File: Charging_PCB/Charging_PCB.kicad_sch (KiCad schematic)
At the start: 15 parts, among them K3 BMS_Relay, K4 IMD_Relay, Q1 PMOS, Q2 PMOS, U112 Charger Input, U113 Signal Inputs, U114 Relay Output

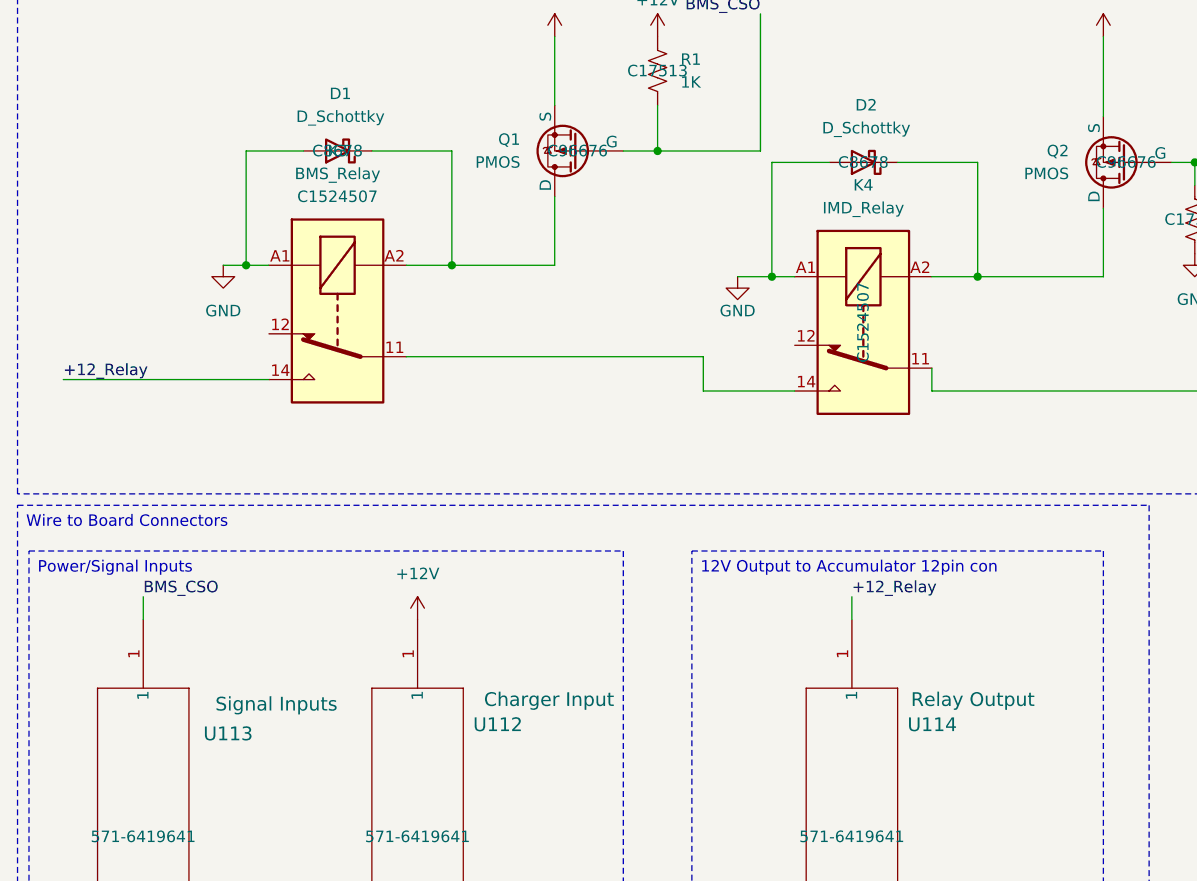
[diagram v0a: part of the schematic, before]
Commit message: Compacted PCB, and finished BOM,CPL,Gerbers(Charging)
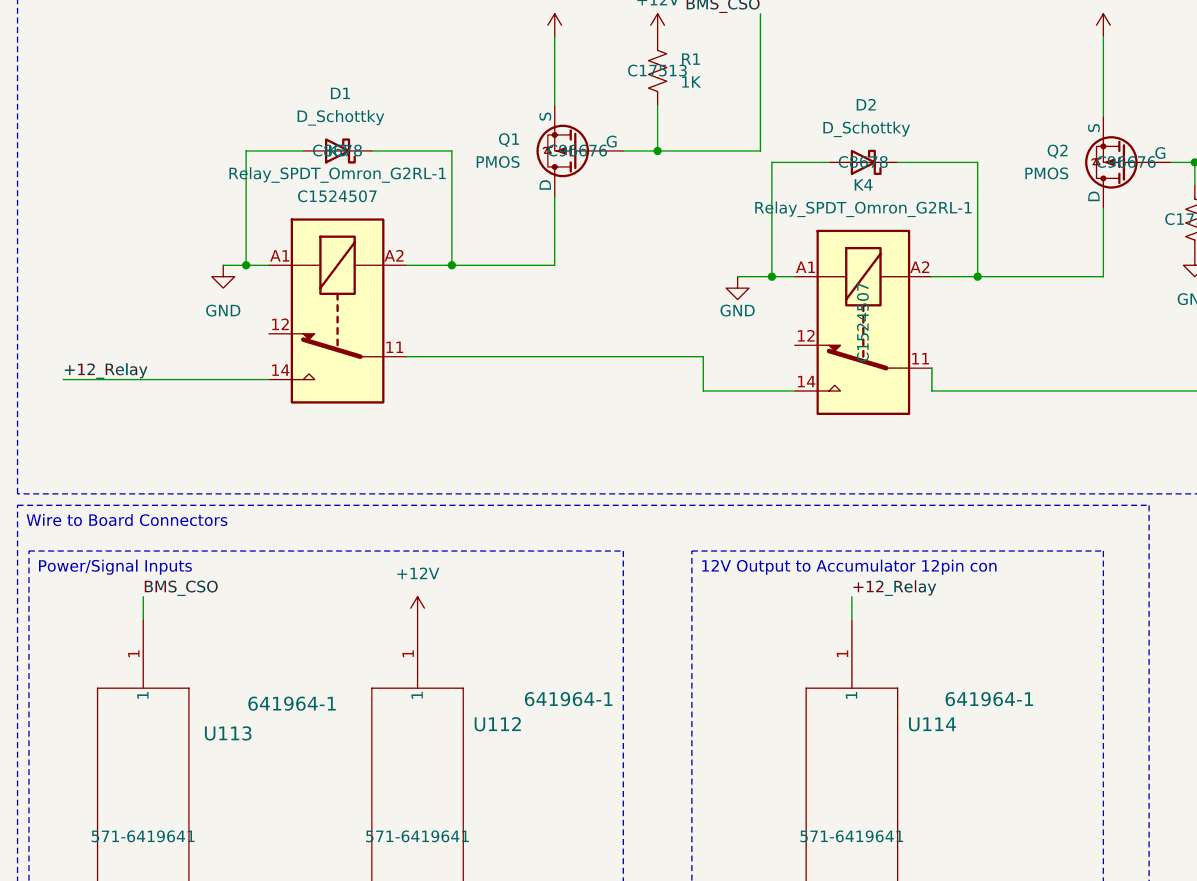
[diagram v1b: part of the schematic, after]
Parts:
- K3: value BMS_Relay -> Relay_SPDT_Omron_G2RL-1
- K4: value IMD_Relay -> Relay_SPDT_Omron_G2RL-1
- U112: value Charger Input -> 641964-1
- U113: value Signal Inputs -> 641964-1
- U114: value Relay Output -> 641964-1
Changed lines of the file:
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@@
 			)
 		)
-		(property "Value" "BMS_Relay"
+		(property "Value" "Relay_SPDT_Omron_G2RL-1"
 			(at 58.42 46.99 90)
 			(effects
@@
 			)
 		)
-		(property "Value" "Relay Output"
+		(property "Value" "641964-1"
 			(at 135.89 105.41 90)
 			(effects
@@
 			)
 		)
-		(property "Value" "IMD_Relay"
+		(property "Value" "Relay_SPDT_Omron_G2RL-1"
 			(at 116.84 50.8 90)
 			(effects
@@
 			)
 		)
-		(property "Value" "Signal Inputs"
+		(property "Value" "641964-1"
 			(at 58.42 105.918 90)
 			(effects
@@
 			)
 		)
-		(property "Value" "Charger Input"
+		(property "Value" "641964-1"
 			(at 89.154 105.41 90)
 			(effects

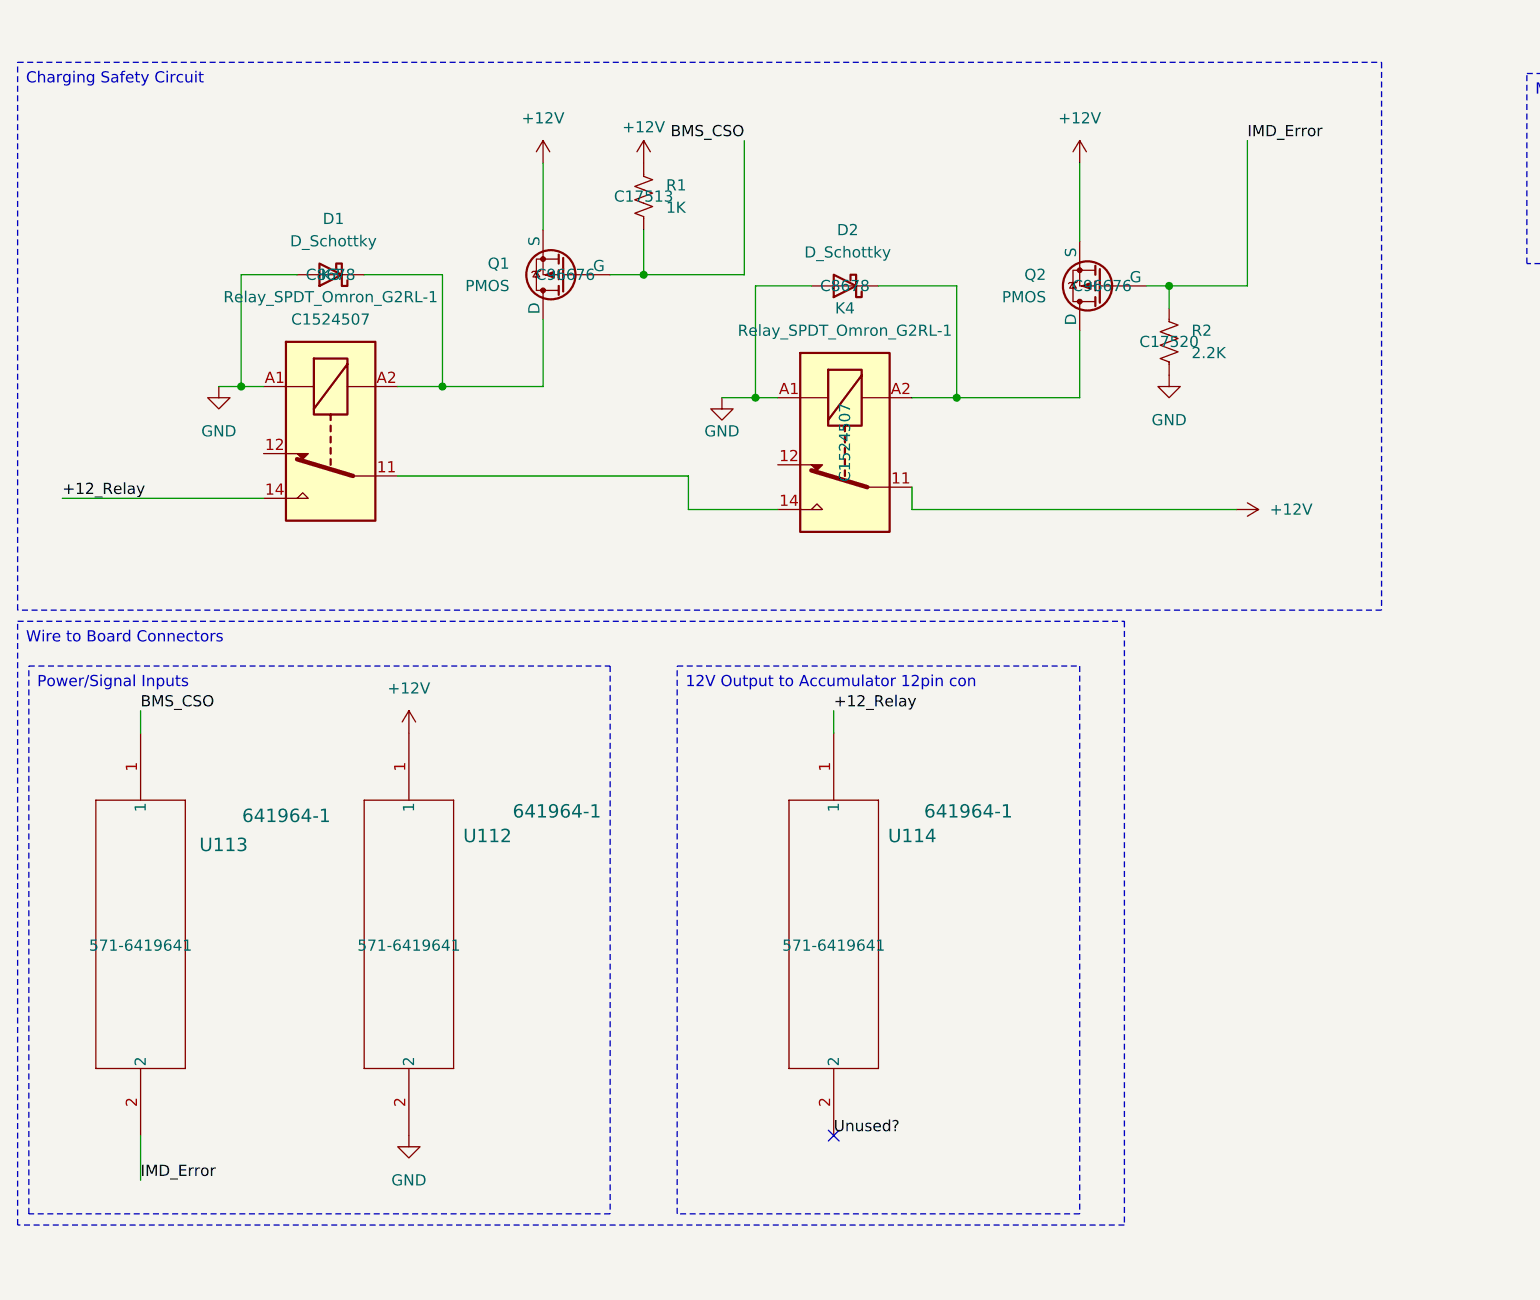
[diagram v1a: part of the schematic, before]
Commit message: Fixed bad PMOS footprint and symbol, fixed gerbers/BOM/CPL
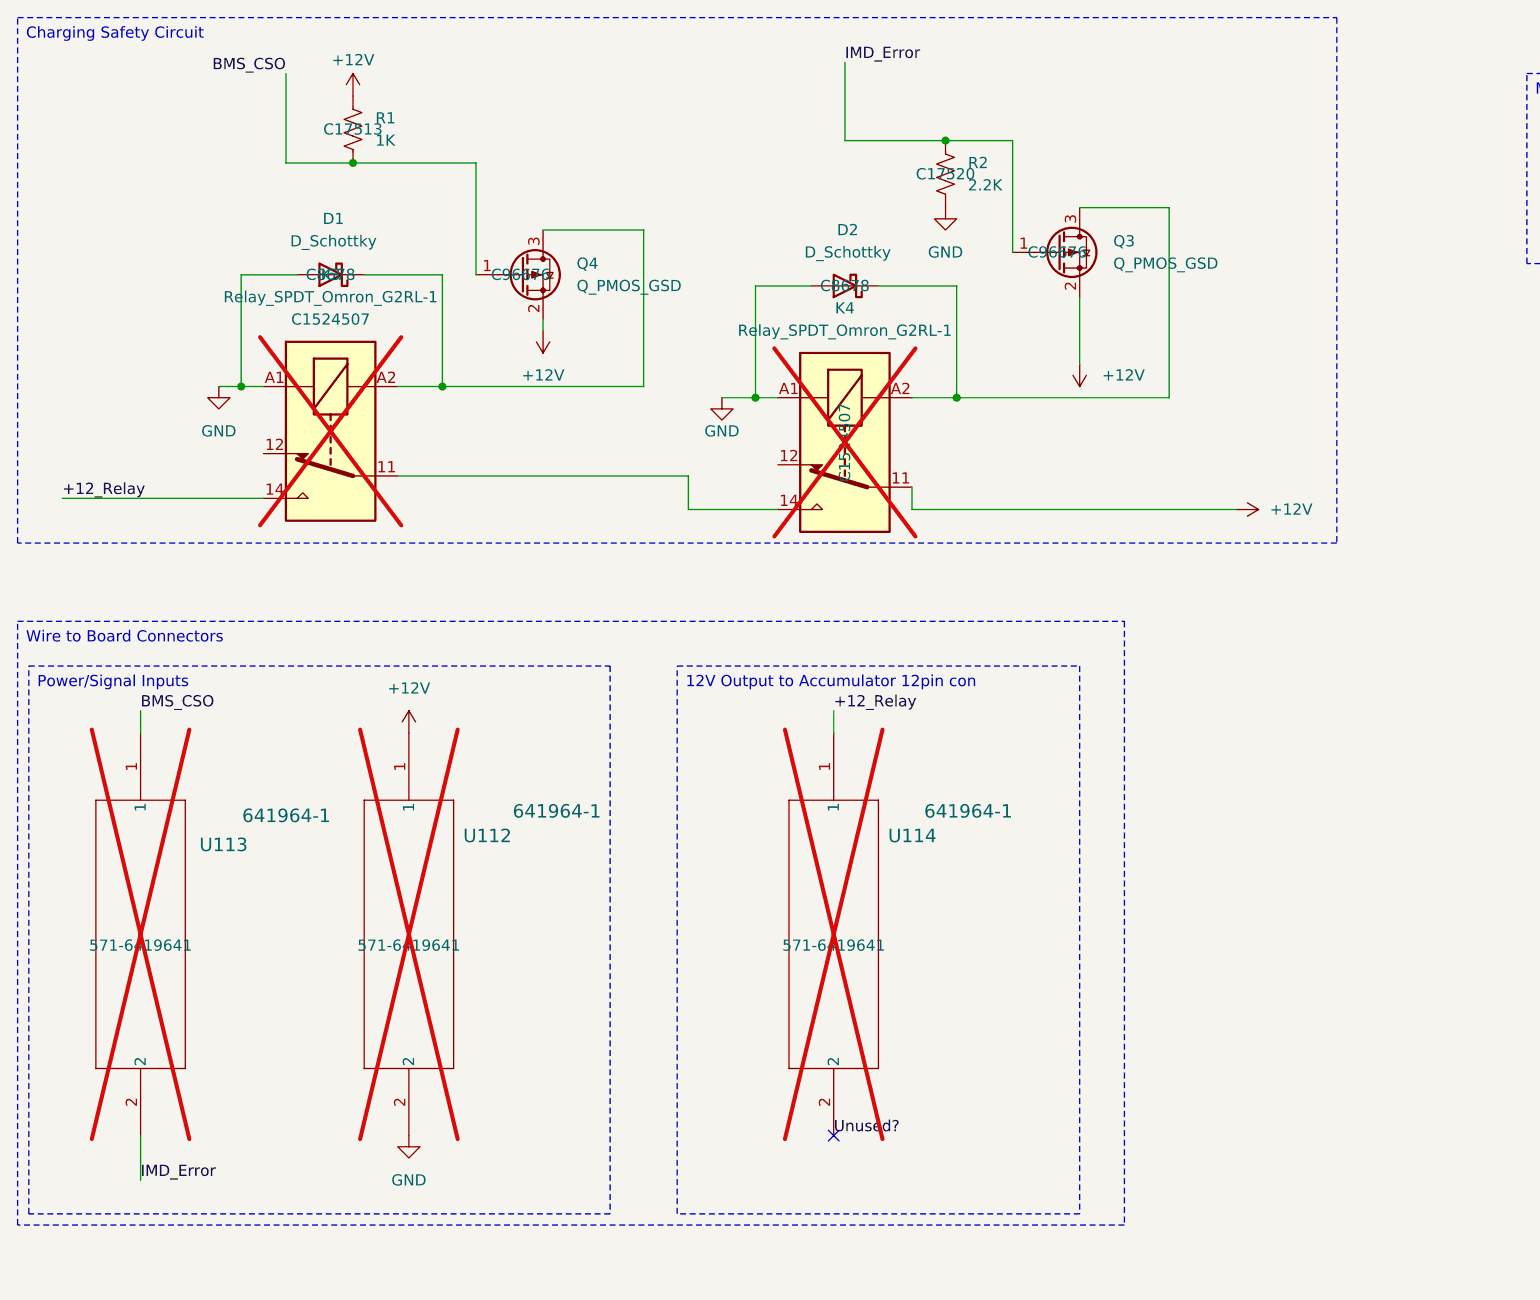
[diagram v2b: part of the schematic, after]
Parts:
- removed Q1, Q2: PMOS, Package_TO_SOT_SMD:SOT-523, symbol Simulation_SPICE:PMOS
- added Q3, Q4: Q_PMOS_GSD, Library:SOT-523_Custom(C96676), symbol Transistor_FET:Q_PMOS_GSD
- K3, K4, U112, U113, U114: now not fitted; now left out of the parts list
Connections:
- net +12V: now also Q3.2 (S), Q4.2 (S)
- net BMS_CSO: now also Q4.1 (G)
- net IMD_Error: now also Q3.1 (G)
- net at D1.1 (K), K3.A2: now also Q4.3 (D)
- net at D2.1 (K), K4.A2: now also Q3.3 (D)
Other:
- moved on the sheet: R1, R2

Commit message: CHARGE READY
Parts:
- H101, H104: now not fitted
- H102: renamed from H103; now not fitted
- H103: renamed from H102; now not fitted
- K101: renamed from K3; now fitted; now in the parts list
- K102: renamed from K4; now fitted; now in the parts list
- renumbered D1 to D101, D2 to D102, Q4 to Q101, Q3 to Q102, R1 to R101, R2 to R102, U113 to U101, U112 to U102, U114 to U103
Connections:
- no-connect marks 1 -> 3
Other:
- moved on the sheet: D102, Q102, R101, R102

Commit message: Finished schematic with added SR latch and new buttons, started layout
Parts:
- added C1, C117, C2: 100n, Capacitor_SMD:C_0603_1608Metric_Pad1.08x0.95mm_HandSolder, symbol Device:C
- added C101, C102: 10n, Capacitor_SMD:C_0603_1608Metric_Pad1.08x0.95mm_HandSolder, symbol Device:C
- added C105: 0.33u, Capacitor_SMD:C_0402_1005Metric, symbol Device:C
- added C106: 0.01u, Capacitor_SMD:C_0402_1005Metric, symbol Device:C
- added D1, D2: LED, LED_SMD:LED_0805_2012Metric_Pad1.15x1.40mm_HandSolder, symbol Device:LED
- added Q1, Q2: NMOS, Package_TO_SOT_SMD:TO-252-2, symbol Simulation_SPICE:NMOS
- added Q103, Q104, Q105, Q106: Q_NPN_BEC, Package_TO_SOT_SMD:SOT-23, symbol Transistor_BJT:Q_NPN_BEC
- added Q107, Q108: Q_PMOS_GSD, Library:SOT-523_Custom(C96676), symbol Transistor_FET:Q_PMOS_GSD
- added R1, R105, R106, R2, R5, R6: 10k, Resistor_SMD:R_0805_2012Metric_Pad1.20x1.40mm_HandSolder, symbol Device:R_US
- added R103, R104, R110, R112: 100k, Resistor_SMD:R_0805_2012Metric_Pad1.20x1.40mm_HandSolder, symbol Device:R_US
- added R108, R109, R111, R113: 1k, Resistor_SMD:R_0805_2012Metric_Pad1.20x1.40mm_HandSolder, symbol Device:R_US
- added R3, R4: 270, Resistor_SMD:R_0805_2012Metric_Pad1.20x1.40mm_HandSolder, symbol Device:R_US
- added SW101, SW102: SW_Omron_B3FS, Button_Switch_SMD:SW_SPST_Omron_B3FS-100xP, symbol Switch:SW_Omron_B3FS
- added U1, U2: SFH617A-1, Package_DIP:DIP-4_W7.62mm, symbol Isolator:SFH617A-1
- added U107: LM7805_TO220, Package_TO_SOT_THT:TO-220-3_Vertical, symbol Regulator_Linear:LM7805_TO220
- added U3, U4: 74AHC1G00, Package_TO_SOT_SMD:SOT-23-5, symbol 74xGxx:74AHC1G00
- added U5: 74LS279, Package_SO:SOIC-16_3.9x9.9mm_P1.27mm, symbol 74xx:74LS279
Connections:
- net +12V: now also D101.1 (K), D102.1 (K), K101.A2, K102.A2, C105.1, Q107.2 (S), Q108.2 (S), U107.1 (VI)
- net BMS_CSO: now also Q107.1 (G); no longer Q101.1 (G)
- net GND: now also C1.2, C105.2, C106.2, C117.2, C2.2, Q1.3 (S), Q103.2 (E), Q104.2 (E), Q105.2 (E), Q106.2 (E), Q2.3 (S), R103.2, R104.2, R5.2, R6.2, U1.2, U1.3, U107.2 (GND), U2.2, U2.3, U3.5 (VCC), U4.5 (VCC), U5.8 (GND); no longer D101.2 (A), D102.2 (A), K101.A1, K102.A1
- net IMD_Error: now also Q108.1 (G); no longer Q102.1 (G)
- new net: C101.2, Q104.1 (B), R110.2
- new net: Q105.1 (B), R106.1
- new net: R104.1, R106.2, SW102.1
- new net: C102.1, Q105.3 (C), R109.2
- new net: C102.2, Q106.1 (B), R112.2
- new net: U4.4, U5.2 (~{S}), U5.3 (~{S})
- new net: D1.1 (K), Q1.2 (G), U5.4 (Q)
- new net: R103.1, R105.2, SW101.1
- new net: D1.2 (A), R3.2
- new net: D101.2 (A), K101.A1, Q1.1 (D)
- new net: Q103.1 (B), R105.1
- new net: C101.1, Q103.3 (C), R108.2
- new net: D102.2 (A), K102.A1, Q2.1 (D)
- new net: D2.1 (K), Q2.2 (G), U5.9 (Q)
- new net: R2.2, U2.4, U3.2
- new net: U3.4, U5.11 (~{S}), U5.12 (~{S})
- new net: D2.2 (A), R4.2
- new net: R1.2, U1.4, U4.2
- new net: Q102.1 (G), Q108.3 (D), R6.1
- new net: Q102.3 (D), U2.1
- new net: Q101.1 (G), Q107.3 (D), R5.1
- new net: Q101.3 (D), U1.1
- new net +5V: C1.1, C106.1, C117.1, C2.1, R1.1, R108.1, R109.1, R110.1, R111.1, R112.1, R113.1, R2.1, R3.1, R4.1, SW101.2, SW102.2, U107.3 (VO), U3.3 (GND), U4.3 (GND), U5.16 (VCC)
- new net BMS_RESET: Q104.3 (C), R111.2, U4.1, U5.1 (~{R})
- new net IMD_RESET: Q106.3 (C), R113.2, U3.1, U5.10 (~{R})
- no-connect marks 3 -> 9
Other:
- note added: "https://tinyurl.com/2486t637"
- moved on the sheet: D101, D102, H101, H102, H103, H104, K101, K102, Q101, Q102, R101, R102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
